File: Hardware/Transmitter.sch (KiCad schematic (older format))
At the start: 15 parts

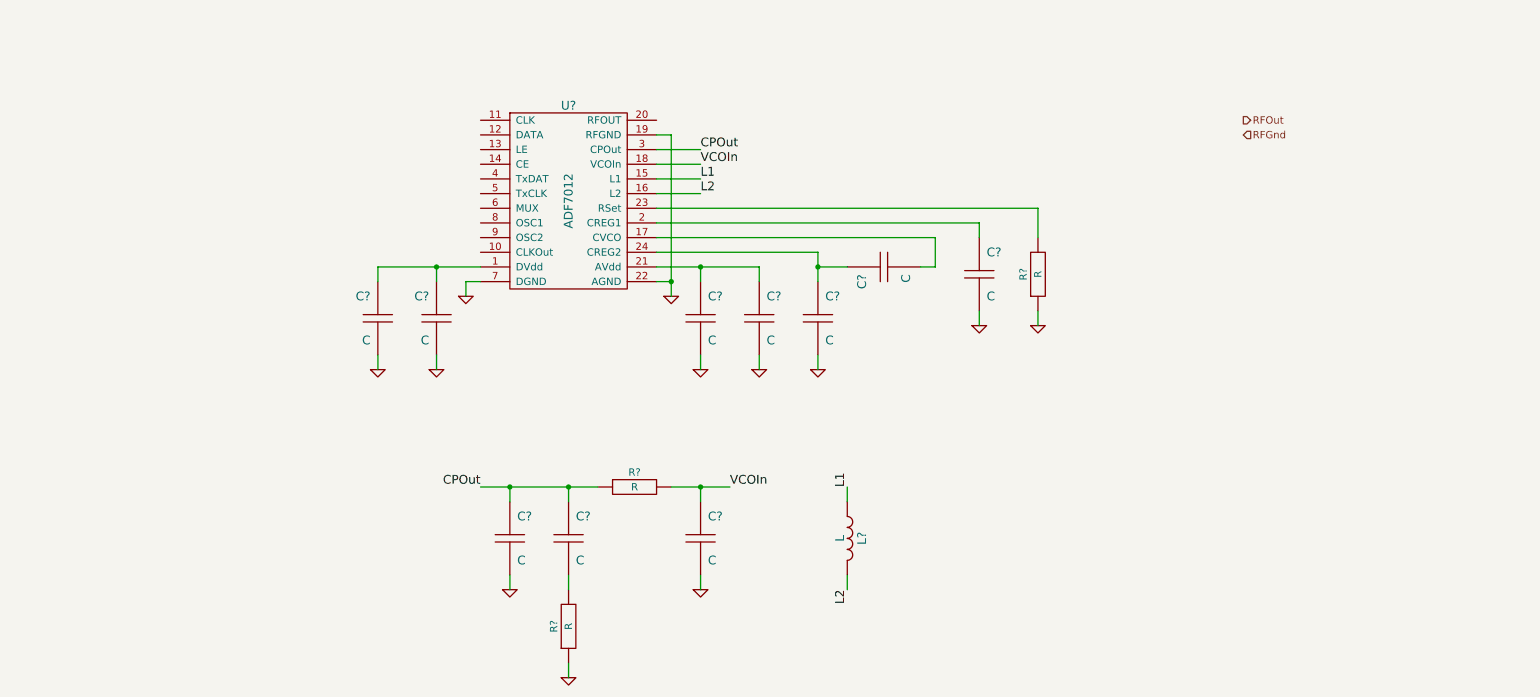
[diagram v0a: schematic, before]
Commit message: More schematic layout
GPS mostly finished
Additional transmitter layout
Core added
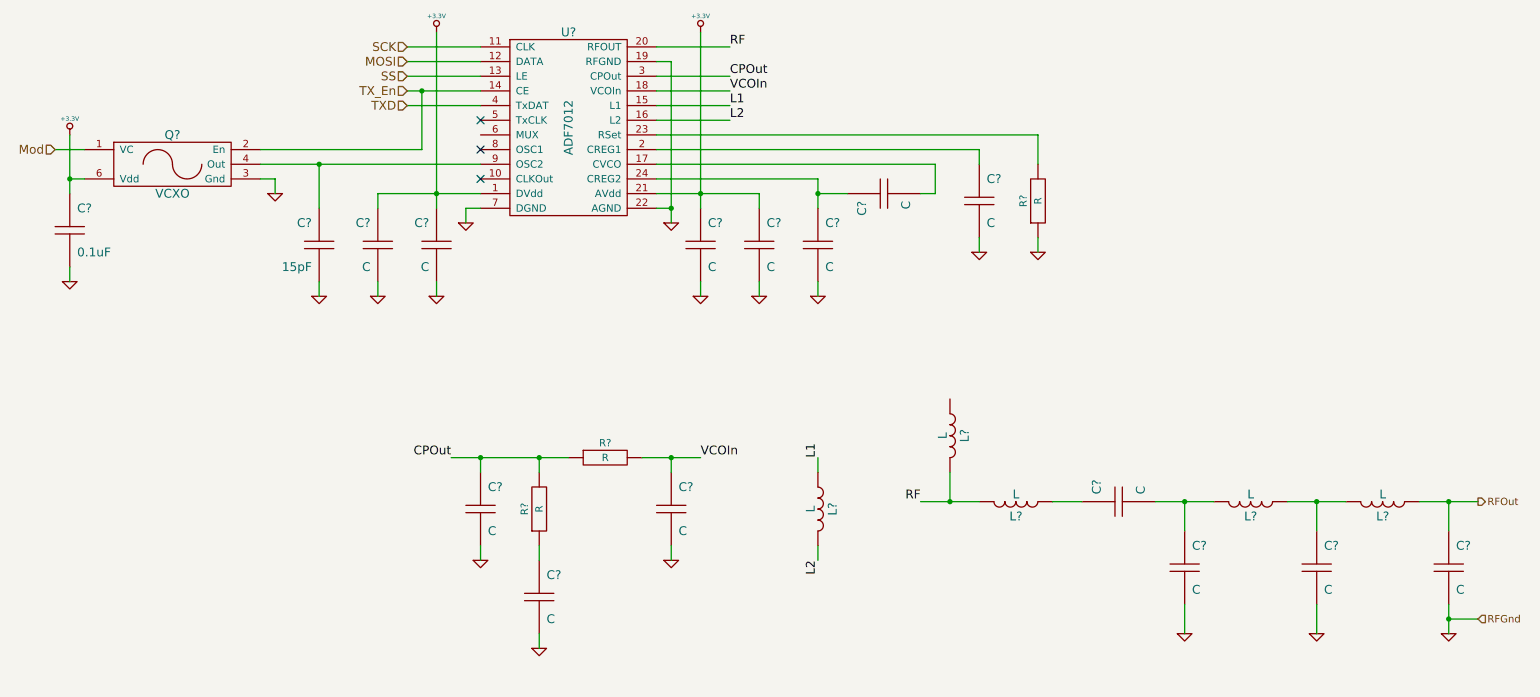
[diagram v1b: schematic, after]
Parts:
- added C? (x4): C, ~, symbol C
- added C?: 0.1uF, ~, symbol C
- added C?: 15pF, ~, symbol C
- added L? (x4): L, ~, symbol L
- added Q?: VCXO, symbol VCXO
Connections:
- net CPOut: now also R?.2; no longer C?.1
- net GND: now also C?.2, C?.2, C?.2, C?.2, C?.2, C?.2, Q?.3 (Gnd); no longer R?.1
- net RFOut: now also C?.1, L?.2
- net +3.3V: now reaches C?.1, C?.1, U?.1 (DVdd)
- net +3.3V: now also C?.1, C?.1, U?.21 (AVdd), C?.1, Q?.6 (Vdd)
- net SCK: now reaches U?.11 (CLK)
- net MOSI: now reaches U?.12 (DATA)
- net SS: now reaches U?.13 (LE)
- net TX_En: now reaches U?.14 (CE)
- net TX_En: now also Q?.2 (En)
- net RF: now reaches U?.20 (RFOUT)
- net RF: now also L?.1, L?.1
- net TXD: now reaches U?.4 (TxDAT)
- net at U?.9 (OSC2): now also C?.1, Q?.4 (Out)
- new net: C?.1, R?.1
- new net: C?.1, L?.2
- new net: C?.1, C?.2, L?.1
- new net: C?.1, L?.1, L?.2
- new net Mod: Q?.1 (VC)
- no-connect marks 0 -> 3
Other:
- moved on the sheet: C?, L?, R?, U?

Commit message: Something changed
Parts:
- removed C?: 0.1uF, ~, symbol C
- added C8: 0.1uF, CAPC1608-N, symbol C
- X1: renamed from Q?; footprint (none) -> OSCSC254P750X520-6N; Distributor Part No (none) -> 631-1302-1-ND; MFR Name (none) -> Fox; MFR Part No (none) -> FVXO-HC73BR-24.576
- gave numbers to parts that had none: 24
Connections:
- net +3.3V: now also L4.2, C8.1
- net GND: now also C8.2

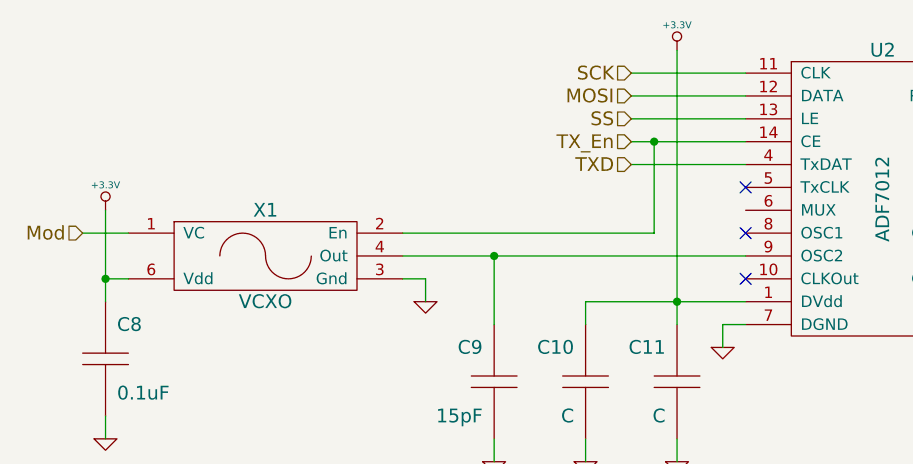
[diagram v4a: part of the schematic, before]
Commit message: Add expansion headers
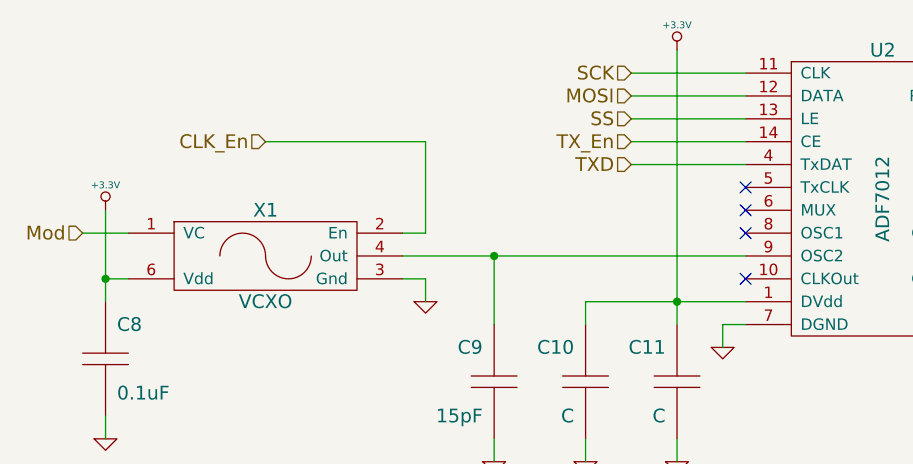
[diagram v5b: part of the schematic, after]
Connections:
- net TX_En: no longer X1.2 (En)
- new net CLK_En: X1.2 (En)
- no-connect marks 3 -> 4
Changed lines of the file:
@@
 Sheet 3 4
 Title "Aether - Pico Tracker"
-Date "4 feb 2014"
+Date "5 feb 2014"
 Rev "1"
 Comp "Aerodyne Labs"
@@
 $EndComp
 $Comp
-L GND #PWR020
+L GND #PWR023
 U 1 1 52E9CB64
 P 7700 4000
-F 0 "#PWR020" H 7700 4000 30  0001 C CNN
+F 0 "#PWR023" H 7700 4000 30  0001 C CNN
 F 1 "GND" H 7700 3930 30  0001 C CNN
 F 2 "" H 7700 4000 60  0000 C CNN
@@
 $EndComp
 $Comp
-L GND #PWR021
+L GND #PWR024
 U 1 1 52E9CBA5
 P 7300 4000
-F 0 "#PWR021" H 7300 4000 30  0001 C CNN
+F 0 "#PWR024" H 7300 4000 30  0001 C CNN
 F 1 "GND" H 7300 3930 30  0001 C CNN
 F 2 "" H 7300 4000 60  0000 C CNN
@@
 $EndComp
 $Comp
-L GND #PWR022
+L GND #PWR025
 U 1 1 52E9CC40
 P 5200 3800
-F 0 "#PWR022" H 5200 3800 30  0001 C CNN
+F 0 "#PWR025" H 5200 3800 30  0001 C CNN
 F 1 "GND" H 5200 3730 30  0001 C CNN
 F 2 "" H 5200 3800 60  0000 C CNN
@@
 $EndComp
 $Comp
-L GND #PWR023
+L GND #PWR026
 U 1 1 52E9CCBC
 P 3800 3800
-F 0 "#PWR023" H 3800 3800 30  0001 C CNN
+F 0 "#PWR026" H 3800 3800 30  0001 C CNN
 F 1 "GND" H 3800 3730 30  0001 C CNN
 F 2 "" H 3800 3800 60  0000 C CNN
@@
 VCOIn
 $Comp
-L GND #PWR024
+L GND #PWR027
 U 1 1 52E9CEED
 P 5200 6100
-F 0 "#PWR024" H 5200 6100 30  0001 C CNN
+F 0 "#PWR027" H 5200 6100 30  0001 C CNN
 F 1 "GND" H 5200 6030 30  0001 C CNN
 F 2 "" H 5200 6100 60  0000 C CNN
@@
 $EndComp
 $Comp
-L GND #PWR025
+L GND #PWR028
 U 1 1 52E9CEFC
 P 3900 6100
-F 0 "#PWR025" H 3900 6100 30  0001 C CNN
+F 0 "#PWR028" H 3900 6100 30  0001 C CNN
 F 1 "GND" H 3900 6030 30  0001 C CNN
 F 2 "" H 3900 6100 60  0000 C CNN
@@
 $EndComp
 $Comp
-L GND #PWR026
+L GND #PWR029
 U 1 1 52E9CF0B
 P 4300 6700
-F 0 "#PWR026" H 4300 6700 30  0001 C CNN
+F 0 "#PWR029" H 4300 6700 30  0001 C CNN
 F 1 "GND" H 4300 6630 30  0001 C CNN
 F 2 "" H 4300 6700 60  0000 C CNN
@@
 L2
 $Comp
-L GND #PWR027
+L GND #PWR030
 U 1 1 52E9D024
 P 3200 4300
-F 0 "#PWR027" H 3200 4300 30  0001 C CNN
+F 0 "#PWR030" H 3200 4300 30  0001 C CNN
 F 1 "GND" H 3200 4230 30  0001 C CNN
 F 2 "" H 3200 4300 60  0000 C CNN
@@
 $EndComp
 $Comp
-L GND #PWR028
+L GND #PWR031
 U 1 1 52E9D033
 P 3600 4300
-F 0 "#PWR028" H 3600 4300 30  0001 C CNN
+F 0 "#PWR031" H 3600 4300 30  0001 C CNN
 F 1 "GND" H 3600 4230 30  0001 C CNN
 F 2 "" H 3600 4300 60  0000 C CNN
@@
 $EndComp
 $Comp
-L GND #PWR029
+L GND #PWR032
 U 1 1 52E9D042
 P 5400 4300
-F 0 "#PWR029" H 5400 4300 30  0001 C CNN
+F 0 "#PWR032" H 5400 4300 30  0001 C CNN
 F 1 "GND" H 5400 4230 30  0001 C CNN
 F 2 "" H 5400 4300 60  0000 C CNN
@@
 $EndComp
 $Comp
-L GND #PWR030
+L GND #PWR033
 U 1 1 52E9D051
 P 5800 4300
-F 0 "#PWR030" H 5800 4300 30  0001 C CNN
+F 0 "#PWR033" H 5800 4300 30  0001 C CNN
 F 1 "GND" H 5800 4230 30  0001 C CNN
 F 2 "" H 5800 4300 60  0000 C CNN
@@
 $EndComp
 $Comp
-L GND #PWR031
+L GND #PWR034
 U 1 1 52E9D060
 P 6200 4300
-F 0 "#PWR031" H 6200 4300 30  0001 C CNN
+F 0 "#PWR034" H 6200 4300 30  0001 C CNN
 F 1 "GND" H 6200 4230 30  0001 C CNN
 F 2 "" H 6200 4300 60  0000 C CNN
@@
 $EndComp
 $Comp
-L GND #PWR032
+L GND #PWR035
 U 1 1 52ECC4BB
 P 8700 6600
-F 0 "#PWR032" H 8700 6600 30  0001 C CNN
+F 0 "#PWR035" H 8700 6600 30  0001 C CNN
 F 1 "GND" H 8700 6530 30  0001 C CNN
 F 2 "" H 8700 6600 60  0000 C CNN
@@
 $EndComp
 $Comp
-L GND #PWR033
+L GND #PWR036
 U 1 1 52ECC4CA
 P 9600 6600
-F 0 "#PWR033" H 9600 6600 30  0001 C CNN
+F 0 "#PWR036" H 9600 6600 30  0001 C CNN
 F 1 "GND" H 9600 6530 30  0001 C CNN
 F 2 "" H 9600 6600 60  0000 C CNN
@@
 $EndComp
 $Comp
-L GND #PWR034
+L GND #PWR037
 U 1 1 52ECC4D9
 P 10500 6600
-F 0 "#PWR034" H 10500 6600 30  0001 C CNN
+F 0 "#PWR037" H 10500 6600 30  0001 C CNN
 F 1 "GND" H 10500 6530 30  0001 C CNN
 F 2 "" H 10500 6600 60  0000 C CNN
@@
 $EndComp
 $Comp
-L +3.3V #PWR035
+L +3.3V #PWR038
 U 1 1 52ED1027
 P 1100 3200
-F 0 "#PWR035" H 1100 3160 30  0001 C CNN
+F 0 "#PWR038" H 1100 3160 30  0001 C CNN
 F 1 "+3.3V" H 1100 3310 30  0000 C CNN
 F 2 "" H 1100 3200 60  0000 C CNN
@@
 $EndComp
 $Comp
-L GND #PWR036
+L GND #PWR039
 U 1 1 52ED10BF
 P 1100 4200
-F 0 "#PWR036" H 1100 4200 30  0001 C CNN
+F 0 "#PWR039" H 1100 4200 30  0001 C CNN
 F 1 "GND" H 1100 4130 30  0001 C CNN
 F 2 "" H 1100 4200 60  0000 C CNN
@@
 $EndComp
 $Comp
-L GND #PWR037
+L GND #PWR040
 U 1 1 52ED1115
 P 2500 3600
-F 0 "#PWR037" H 2500 3600 30  0001 C CNN
+F 0 "#PWR040" H 2500 3600 30  0001 C CNN
 F 1 "GND" H 2500 3530 30  0001 C CNN
 F 2 "" H 2500 3600 60  0000 C CNN
@@
 Wire Wire Line
 	3400 3000 3900 3000
-Wire Wire Line
-	3500 2900 3500 3300
-Wire Wire Line
-	3500 3300 2400 3300
-Connection ~ 3500 2900
 $Comp
 L C C9
@@
 Connection ~ 2800 3400
 $Comp
-L GND #PWR038
+L GND #PWR041
 U 1 1 52ED13E6
 P 2800 4300
-F 0 "#PWR038" H 2800 4300 30  0001 C CNN
+F 0 "#PWR041" H 2800 4300 30  0001 C CNN
 F 1 "GND" H 2800 4230 30  0001 C CNN
 F 2 "" H 2800 4300 60  0000 C CNN
@@
 	2800 4300 2800 4200
 $Comp
-L +3.3V #PWR039
+L +3.3V #PWR042
 U 1 1 52ED145B
 P 3600 2500
-F 0 "#PWR039" H 3600 2460 30  0001 C CNN
+F 0 "#PWR042" H 3600 2460 30  0001 C CNN
 F 1 "+3.3V" H 3600 2610 30  0000 C CNN
 F 2 "" H 3600 2500 60  0000 C CNN
@@
 $EndComp
 $Comp
-L +3.3V #PWR040
+L +3.3V #PWR043
 U 1 1 52ED146A
 P 5400 2500
-F 0 "#PWR040" H 5400 2460 30  0001 C CNN
+F 0 "#PWR043" H 5400 2460 30  0001 C CNN
 F 1 "+3.3V" H 5400 2610 30  0000 C CNN
 F 2 "" H 5400 2500 60  0000 C CNN
@@
 $EndComp
 $Comp
-L +3.3V #PWR?
+L +3.3V #PWR044
 U 1 1 52F05AEA
 P 7100 4800
-F 0 "#PWR?" H 7100 4760 30  0001 C CNN
+F 0 "#PWR044" H 7100 4760 30  0001 C CNN
 F 1 "+3.3V" H 7100 4910 30  0000 C CNN
 F 2 "" H 7100 4800 60  0000 C CNN
@@
 Wire Wire Line
 	7100 4800 7100 5000
+NoConn ~ 3900 3200
+Text HLabel 1800 2900 0    60   Input ~ 0
+CLK_En
+Wire Wire Line
+	1800 2900 2500 2900
+Wire Wire Line
+	2500 2900 2500 3300
+Wire Wire Line
+	2500 3300 2400 3300
 $EndSCHEMATC
